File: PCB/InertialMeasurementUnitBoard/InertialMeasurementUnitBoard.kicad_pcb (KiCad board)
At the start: 2 copper layers, 16 parts, among them J1 1769, J2 2005280060, U1 CD74HC4050PWR, X2 SC32S-7PF20PPM

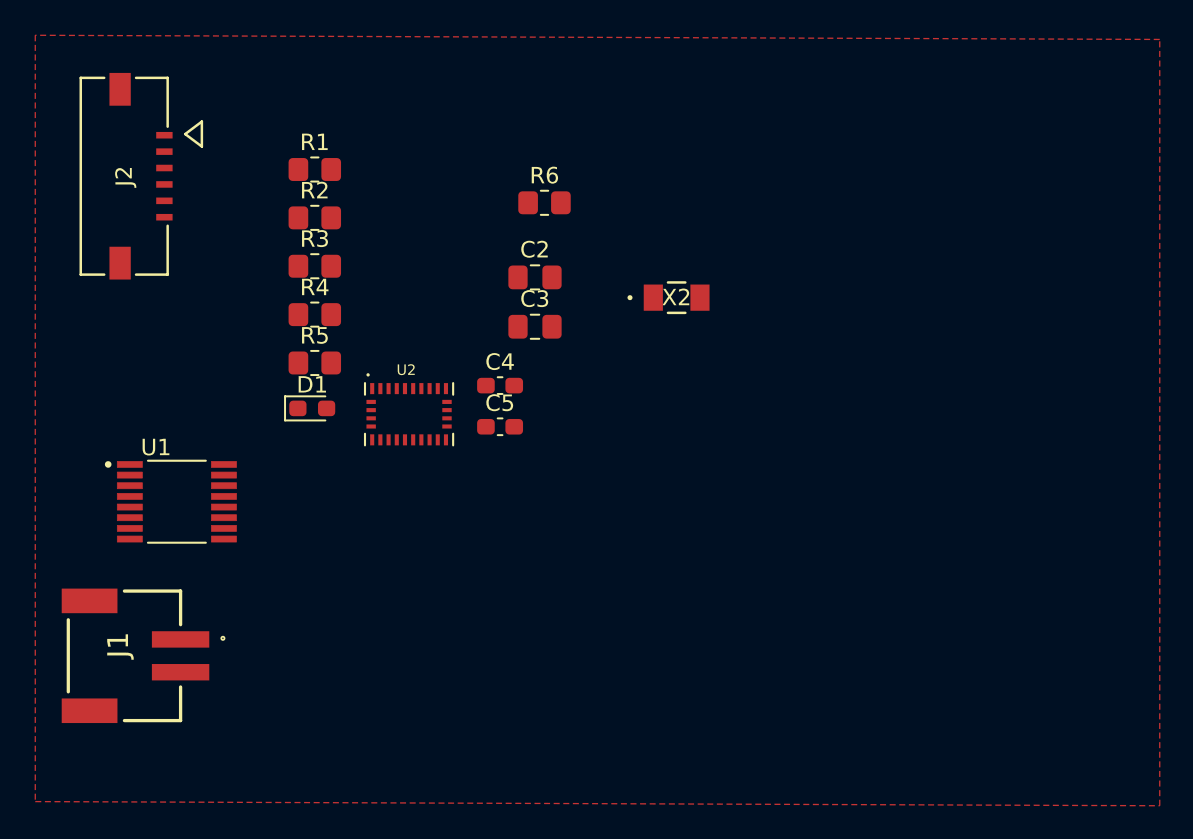
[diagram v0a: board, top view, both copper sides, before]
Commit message: Initial completion of Inertial Measurement Unit Board
Add test points for BMS outputs, complete layout.
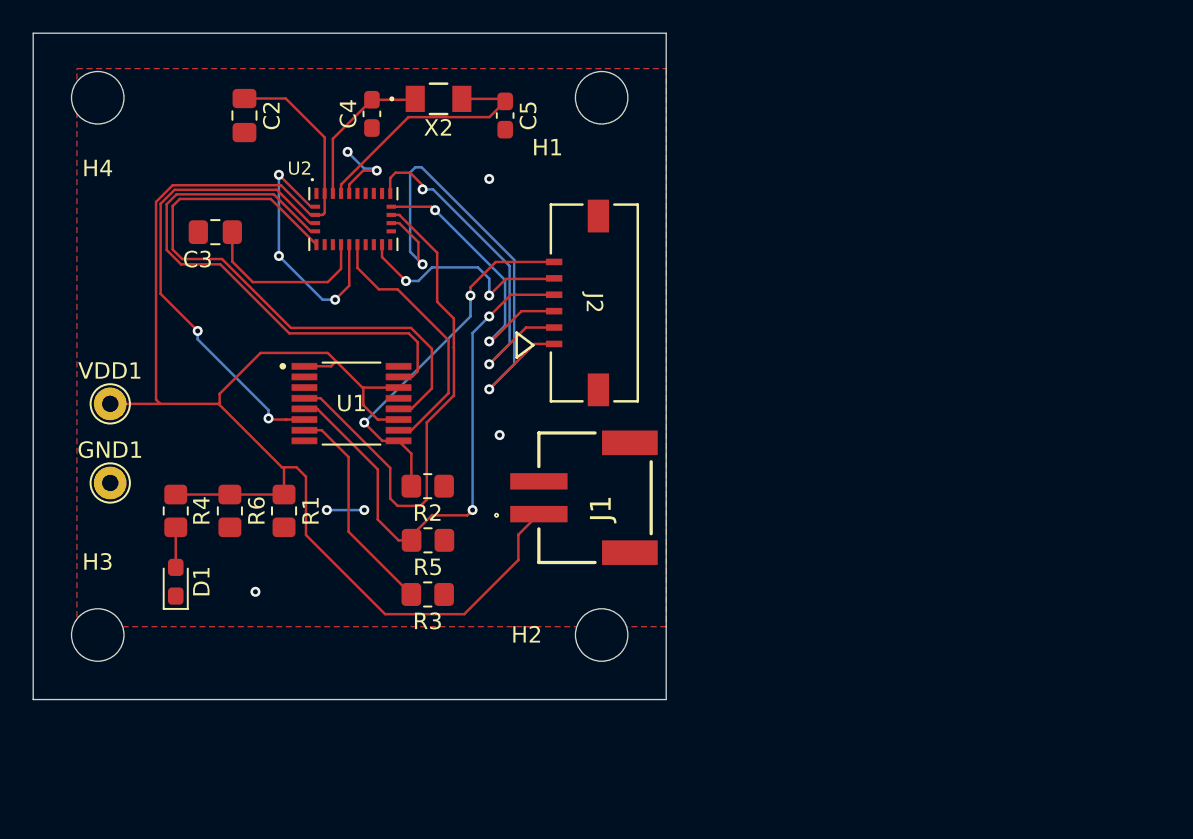
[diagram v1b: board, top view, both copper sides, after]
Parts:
- added GND1: TestPoint, TestPoint:TestPoint_THTPad_D2.0mm_Drill1.0mm, F.Cu at (101.1, 103.5)
- added H1: MountingHole, MountingHole:MountingHole_3.2mm_M3, F.Cu at (131.1, 80.0)
- added H2: MountingHole, MountingHole:MountingHole_3.2mm_M3, F.Cu at (131.1, 112.8)
- added H3: MountingHole, MountingHole:MountingHole_3.2mm_M3, F.Cu at (100.3, 112.8)
- added H4: MountingHole, MountingHole:MountingHole_3.2mm_M3, F.Cu at (100.3, 80.0)
- added VDD1: TestPoint, TestPoint:TestPoint_THTPad_D2.0mm_Drill1.0mm, F.Cu at (101.1, 98.7)
- moved J2 29.7 mm to (130.6, 92.5), turned to 90 degrees
- moved R6 26.9 mm to (108.4, 105.2), turned to -90 degrees
- moved J1 23.9 mm to (127.2, 104.4), turned to 90 degrees
- moved R3 21.2 mm to (120.5, 110.3), turned to 180 degrees
- moved R1 20.9 mm to (111.7, 105.2), turned to -90 degrees
- moved C3 20.3 mm to (107.5, 88.2), turned to 180 degrees
- moved C2 20.3 mm to (109.3, 81.1), turned to -90 degrees
- moved C5 19.0 mm to (125.2, 81.1), turned to -90 degrees
- moved X2 18.9 mm to (121.1, 80.1)
- moved C4 18.3 mm to (117.1, 81.0), turned to -90 degrees
- moved R2 17.8 mm to (120.5, 103.7), turned to 180 degrees
- moved R4 14.7 mm to (105.1, 105.2), turned to 90 degrees
- moved D1 13.5 mm to (105.1, 109.5), turned to 90 degrees
- moved R5 12.8 mm to (120.5, 107.0), turned to 180 degrees
- moved U2 12.4 mm to (115.9, 87.4)
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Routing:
- net +3.3V: track 0.00 -> 98.8 mm
- net /PS0_BUF: track 0.00 -> 36.0 mm
- net /PS1_BUF: track 0.00 -> 33.8 mm
- net /CS_N: track 0.00 -> 33.0 mm, vias 0 -> 2
- net /MOSI: track 0.00 -> 32.3 mm, vias 0 -> 2
- net /CS_N_BUF: track 0.00 -> 31.4 mm
- net /BOOT_N_BUF: track 0.00 -> 28.7 mm, vias 0 -> 2
- net GND: track 0.00 -> 23.5 mm, vias 0 -> 10
- net /MISO: track 0.00 -> 22.6 mm, vias 0 -> 2
- net /RST_N: track 0.00 -> 22.3 mm, vias 0 -> 2
- net /SCLK: track 0.00 -> 18.0 mm, vias 0 -> 2
- net /RST_N_BUF: track 0.00 -> 16.0 mm
- net Net-(U2-CLKSEL1/XOUT32): track 0.00 -> 15.4 mm
- net /INT_N: track 0.00 -> 13.9 mm, vias 0 -> 2
- net Net-(U1-3A): track 0.00 -> 13.3 mm
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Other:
- board outline added: 38.6 x 40.6 mm

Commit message: Small edits to IMU board layout
Tidying up of silkscreen, traces, fab, etc.
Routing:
- net /PS0_BUF: track 36.0 -> 38.4 mm
- net GND: track 23.5 -> 24.1 mm
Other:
- board text added: "PWR"
